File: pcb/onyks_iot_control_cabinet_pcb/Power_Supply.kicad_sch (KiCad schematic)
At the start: 11 parts, among them J1 Screw_Terminal_01x02, J3 Jack-DC, J4 Conn_01x03_Pin, U2 LMR51430

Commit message: New fixes of schematics
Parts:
- L1: value 5.6u -> XAL6060-562MEC_COC
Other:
- moved on the sheet: L1
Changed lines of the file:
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@@
 	(wire
 		(pts
-			(xy 176.53 105.41) (xy 185.42 105.41)
+			(xy 176.53 105.41) (xy 194.31 105.41)
 		)
 		(stroke
@@
 	(wire
 		(pts
-			(xy 193.04 105.41) (xy 205.74 105.41)
+			(xy 201.93 105.41) (xy 205.74 105.41)
 		)
 		(stroke
@@
 		)
 	)
-	(text_box "V_OUT = 3.3 V\nI_OUT_MAX = 2 A\n\nV_IN = 9V\n	I_IN_AVG = 800 mA\n	PWR_DISSIPATION = 600 mW\n\nV_IN = 12V\n	I_IN_AVG = 650 mA\n	PWR_DISSIPATION =  650 mW\n\nV_IN = 24V\n	I_IN_AVG = 350 mA\n	PWR_DISSIPATION = 1 W\n"
-		(exclude_from_sim no)
-		(at 201.93 68.58 0)
-		(size 37.465 32.385)
+	(text_box "RANGE OF V_IN: 9 V - 24 V\n* IT DEPENDS OF USED BUZZER AND THE LOCKER WHICH WE WANT TO CONTROL\n\nV_OUT: 3.3 V\nI_OUT_MAX: 2 A\n\nV_IN = 9V\n* I_IN_AVG = 800 mA\n\nV_IN = 12V\n* I_IN_AVG = 650 mA\n\nV_IN = 24V\n* I_IN_AVG = 350 mA\n\nIF WE HAVE THE POWER SUPPLY WITH PARAMETERS:\n* V_POWER_SUPPLY = X\n* I_MAX_POWER_SUPPLY = Y\n\nWE CAN POWER THE LOCK WITH:\n* V_POWER_SUPPLY = X\n* I_LOCK_MAX = I_MAX_POWER_SUPPLY - I_IN_AVG - I_BUZZER_MAX\n"
+		(exclude_from_sim no)
+		(at 19.05 21.59 0)
+		(size 80.01 48.26)
 		(stroke
 			(width 0)
@@
 	(text "MCU Power Supply"
 		(exclude_from_sim no)
-		(at 150.622 56.896 0)
+		(at 150.368 75.946 0)
 		(effects
 			(font
@@
 	(symbol
 		(lib_id "Device:L")
-		(at 189.23 105.41 90)
+		(at 198.12 105.41 90)
 		(unit 1)
 		(exclude_from_sim no)
@@
 		(dnp no)
 		(property "Reference" "L1"
-			(at 189.23 100.33 90)
-			(effects
-				(font
-					(size 1.27 1.27)
-				)
-			)
-		)
-		(property "Value" "5.6u"
-			(at 189.23 102.87 90)
+			(at 198.12 100.33 90)
+			(effects
+				(font
+					(size 1.27 1.27)
+				)
+			)
+		)
+		(property "Value" "XAL6060-562MEC_COC"
+			(at 198.12 102.87 90)
 			(effects
 				(font
@@
 		)
 		(property "Footprint" "ourFootprints:XAL6060-562MEC_COC"
-			(at 189.23 105.41 0)
+			(at 198.12 105.41 0)
 			(effects
 				(font
@@
 		)
 		(property "Datasheet" "~"
-			(at 189.23 105.41 0)
+			(at 198.12 105.41 0)
 			(effects
 				(font
@@
 		)
 		(property "Description" "Inductor"
-			(at 189.23 105.41 0)
-			(effects
-				(font
+			(at 198.12 105.41 0)
+			(effects
+				(font

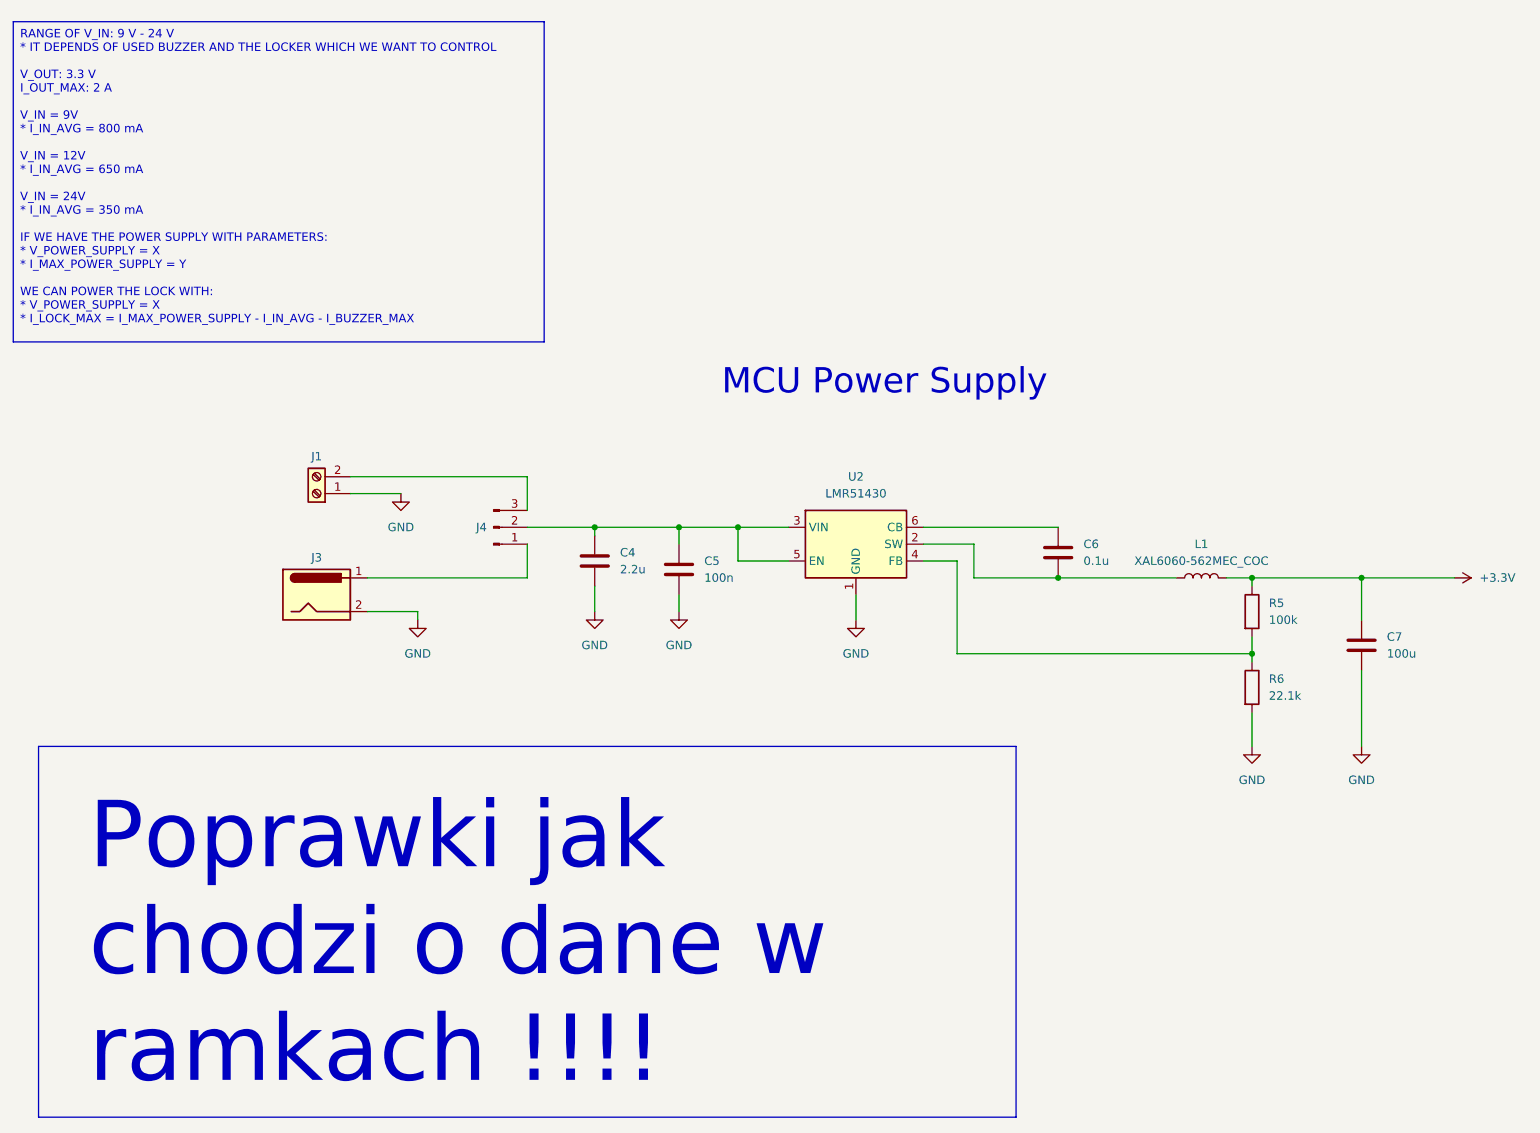
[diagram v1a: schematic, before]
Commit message: Final fixes? - update the power supply
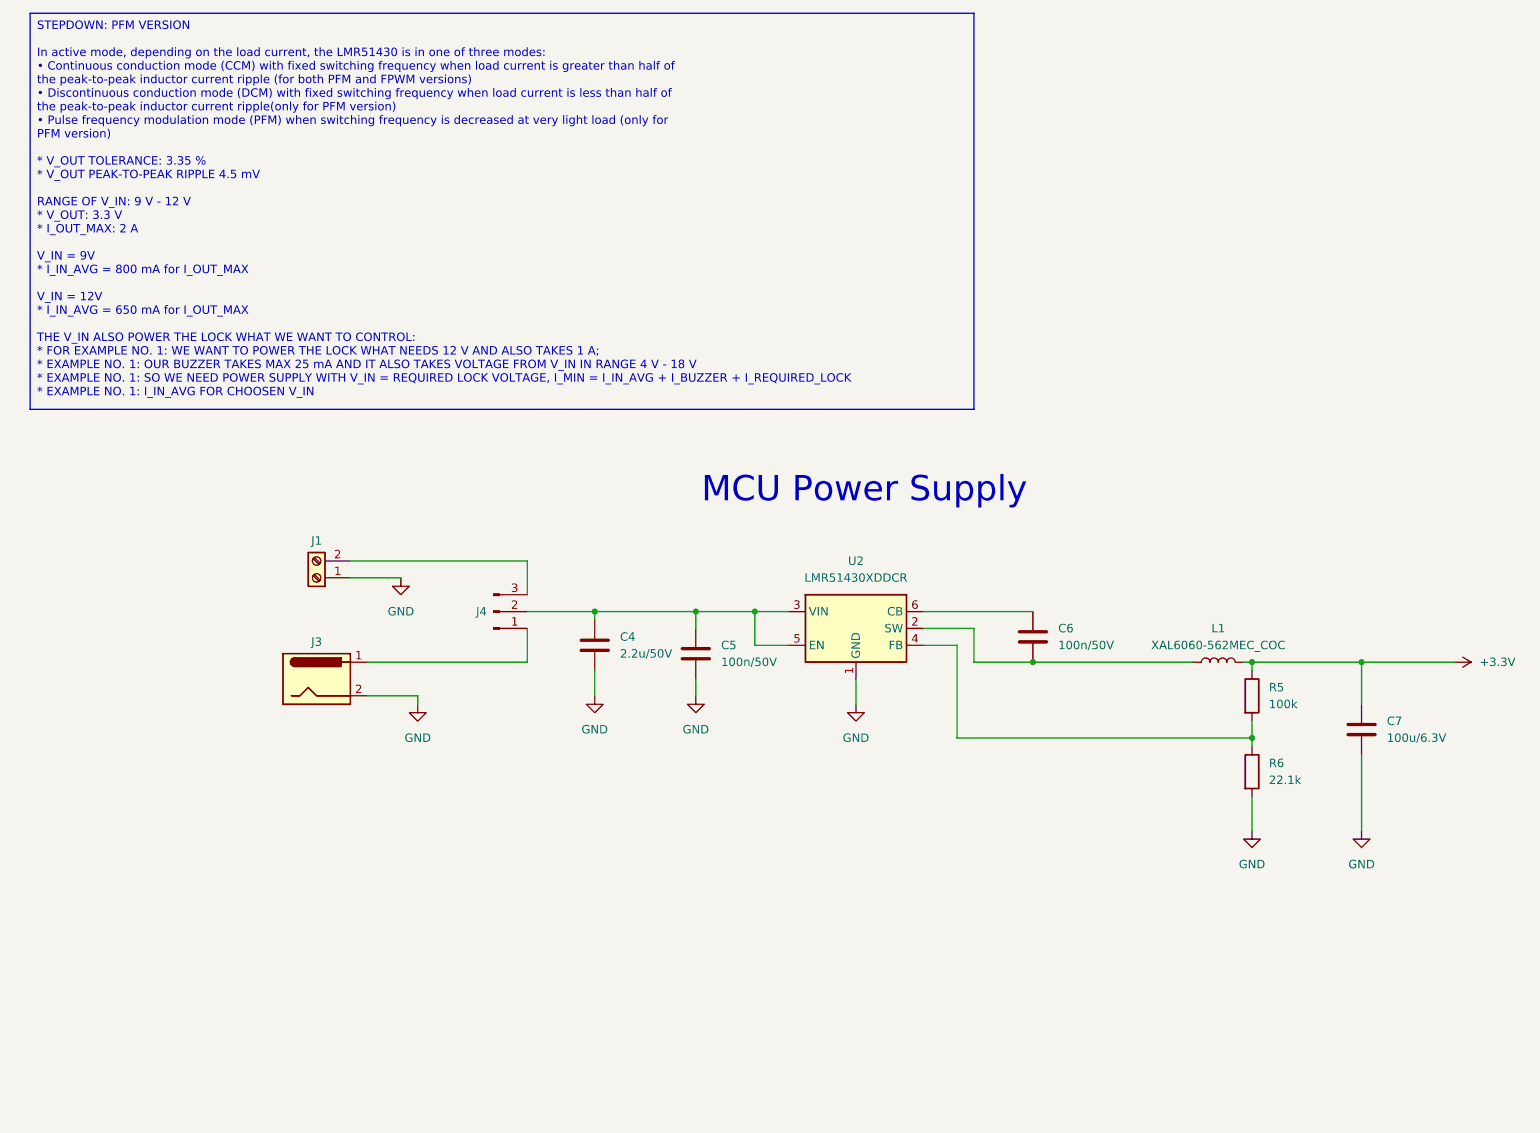
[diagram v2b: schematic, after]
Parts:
- C4: value 2.2u -> 2.2u/50V; footprint Capacitor_SMD:C_0805_2012Metric -> Capacitor_SMD:C_0603_1608Metric
- C5: value 100n -> 100n/50V; footprint Capacitor_SMD:C_0805_2012Metric -> Capacitor_SMD:C_0603_1608Metric
- C6: value 0.1u -> 100n/50V
- C7: value 100u -> 100u/6.3V
- U2: value LMR51430 -> LMR51430XDDCR
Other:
- moved on the sheet: C4, C5, C6, C7, J1, J3, J4, L1, R5, R6, U2
